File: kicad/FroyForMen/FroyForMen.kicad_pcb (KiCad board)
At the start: 2 copper layers, 105.6 x 57 mm, 28 parts, among them IC1 ESP-WROOM-02U__4MB_, J1 Screw_Terminal_01x02, J2 Conn_01x06, Q1 Q_NPN_BEC, Q2 Q_NPN_BEC, Q3 Q_NPN_BEC, Q4 Q_NPN_BEC, SW1 SW_SPST, U1 BME280

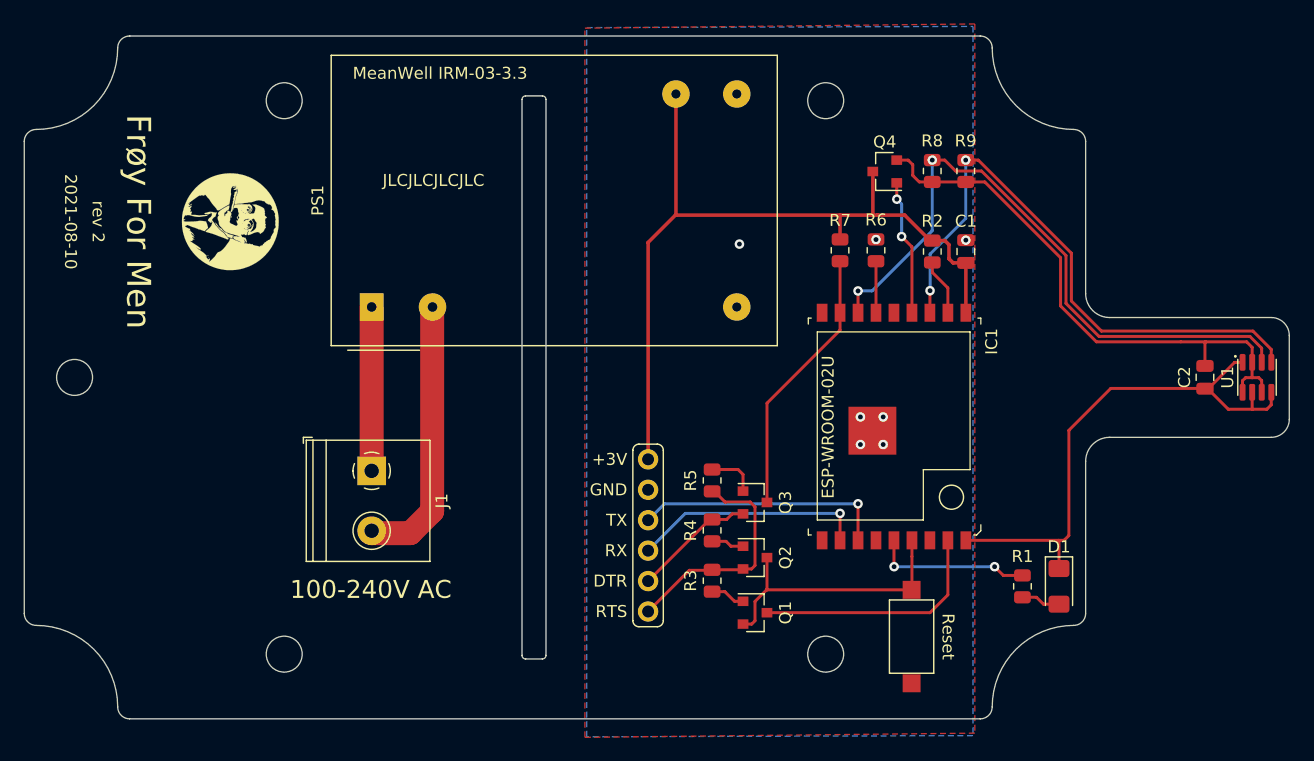
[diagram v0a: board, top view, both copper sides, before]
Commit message: FroyForMen v1.3 - removed power transistor, use Omron button
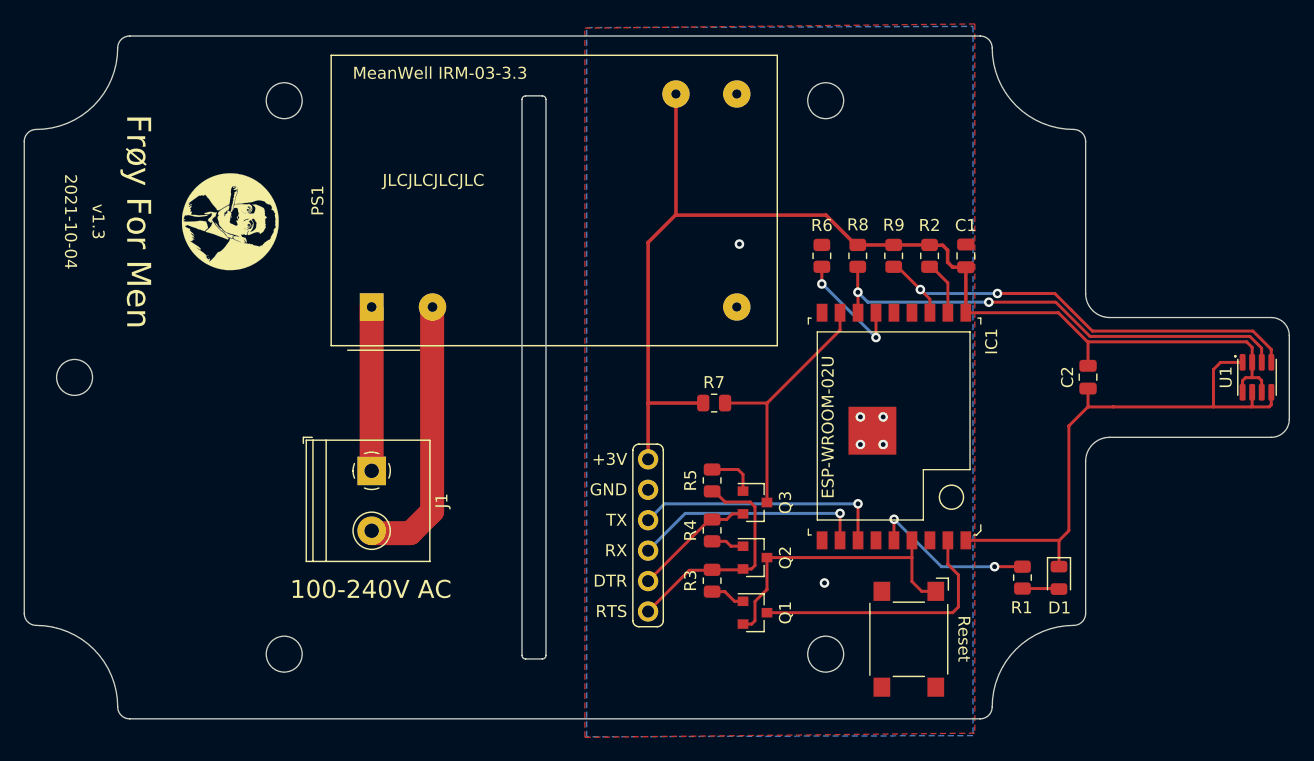
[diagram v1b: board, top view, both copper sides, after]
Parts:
- removed Q4: Q_NPN_BEC, Package_TO_SOT_SMD:SOT-23
- D1: footprint LED_SMD:LED_1206_3216Metric_Pad1.42x1.75mm_HandSolder -> LED_SMD:LED_0805_2012Metric
- R8, R9: value 4k7 -> 10k
- SW1: value SW_SPST -> SW_MEC_5E; footprint Button_Switch_SMD:SW_SPST_CK_RS282G05A3 -> xrstf:SW_SPST_Omron_B3FS-100xP
- moved R7 16.5 mm to (102.2, 56.1), turned to 180 degrees
- moved C2 9.76 mm to (133.4, 54.0)
- moved R8 9.42 mm to (114.2, 43.9), turned to 270 degrees
- moved R9 9.29 mm to (117.2, 43.9), turned to 270 degrees
- moved R6 4.54 mm to (111.2, 43.9)
- moved R1 0.73 mm to (127.9, 70.7)
- moved D1 0.71 mm to (131.0, 70.7)
- moved R2 0.43 mm to (120.2, 43.9)
- moved C1 0.36 mm to (123.2, 43.9)
- moved SW1 0.32 mm to (118.4, 75.9)
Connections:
- C2 pad 2: +3.3VP -> +3V3
- IC1 pad 4: /SENS_PWR -> (no net)
- R8 pad 1: +3.3VP -> +3V3
- R9 pad 1: +3.3VP -> +3V3
- SW1 pad 2: GNDREF -> (no net)
- U1 pad 2: +3.3VP -> +3V3
- U1 pad 6: +3.3VP -> +3V3
- U1 pad 8: +3.3VP -> +3V3
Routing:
- net +3.3VP: track 47.3 -> 0.00 mm
- net +3V3: track 68.0 -> 100.0 mm
- net /I2C_SDA: track 53.5 -> 40.7 mm
- net /I2C_CLK: track 49.5 -> 37.7 mm
- net /SENS_PWR: track 11.4 -> 0.00 mm, vias 2 -> 0
- net Net-(IC1-Pad6): track 4.30 -> 9.88 mm, vias 0 -> 2
- net /WAKE_UP: track 20.3 -> 22.1 mm
- net /RST: track 23.0 -> 24.7 mm
- net GNDREF: track 45.6 -> 47.1 mm, vias 7 -> 6
- net /LED: track 13.2 -> 14.1 mm
- net /IO0: track 22.7 -> 21.9 mm
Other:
- board text added: "2021-10-04"
- board text added: "2k2 10k 10k 10k 10k 10k 10k 10k 10k"
- board text added: "NPN NPN NPN"
- board text added: "Q1 Q2 Q3"
- board text added: "v1.3"
- board text removed: "2021-08-10"
- board text removed: "2k2 10k 10k 10k 10k 10k 10k 4k7 4k7"
- board text removed: "NPN NPN NPN NPN"
- board text removed: "Q1 Q2 Q3 Q4"
- board text removed: "rev 2"
